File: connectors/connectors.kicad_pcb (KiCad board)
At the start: 2 copper layers, 41.7 x 4.8 mm, 15 parts, among them P11 CONN_1, P12 CONN_1, P13 CONN_1, P14 CONN_1, P15 CONN_1, P21 CONN_1, P22 CONN_1, P23 CONN_1, P24 CONN_1, P25 CONN_1

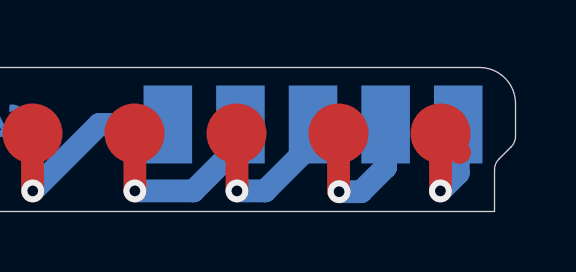
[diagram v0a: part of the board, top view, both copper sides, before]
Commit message: Remove extra track.
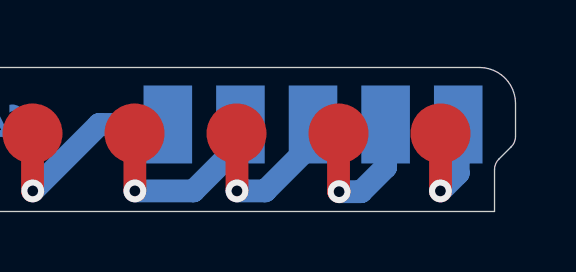
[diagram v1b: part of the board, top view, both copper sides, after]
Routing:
- net N-000005: track 5.27 -> 4.38 mm
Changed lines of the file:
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@@
     (links 5)
     (no_connects 0)
-    (area 108.5 78.745 182.728571 112.4385)
+    (area 108.5 78.745 182.728571 112.7285)
     (thickness 1.6)
     (drawings 25)
-    (tracks 32)
+    (tracks 31)
     (zones 0)
     (modules 15)
@@
   (segment (start 153.7208 108.9892) (end 153.723 108.987) (width 0.762) (layer B.Cu) (net 4))
   (segment (start 155.553 109.287) (end 155.553 111.1978) (width 0.762) (layer F.Cu) (net 5))
+  (segment (start 155.553 111.1978) (end 155.5496 111.2012) (width 0.762) (layer F.Cu) (net 5))
+  (via (at 155.5496 111.2012) (size 0.762) (drill 0.3556) (layers F.Cu B.Cu) (net 5))
+  (segment (start 155.5496 111.2012) (end 156.143 110.6078) (width 0.762) (layer B.Cu) (net 5))
   (segment (start 156.143 110.6078) (end 156.143 108.987) (width 0.762) (layer B.Cu) (net 5))
-  (segment (start 155.5496 111.2012) (end 156.143 110.6078) (width 0.762) (layer B.Cu) (net 5))
-  (via (at 155.5496 111.2012) (size 0.762) (drill 0.3556) (layers F.Cu B.Cu) (net 5))
-  (segment (start 155.553 111.1978) (end 155.5496 111.2012) (width 0.762) (layer F.Cu) (net 5))
-  (segment (start 155.553 109.287) (end 156.1846 109.9186) (width 0.762) (layer F.Cu) (net 5))
 )

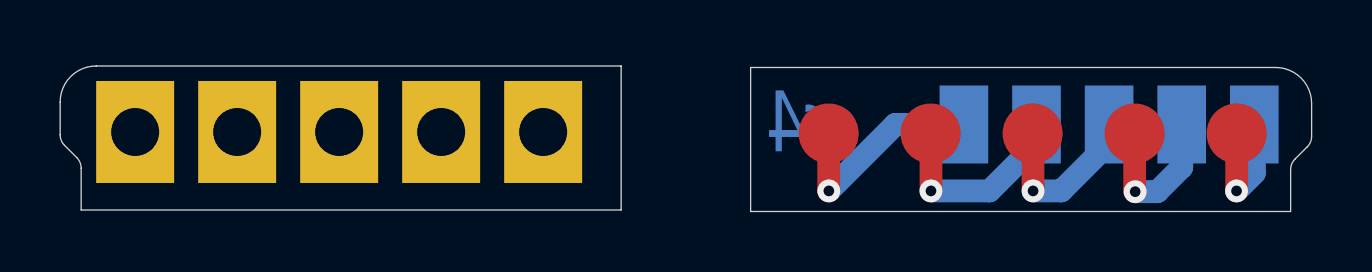
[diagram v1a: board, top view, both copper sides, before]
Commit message: Add drill holes to the connector.
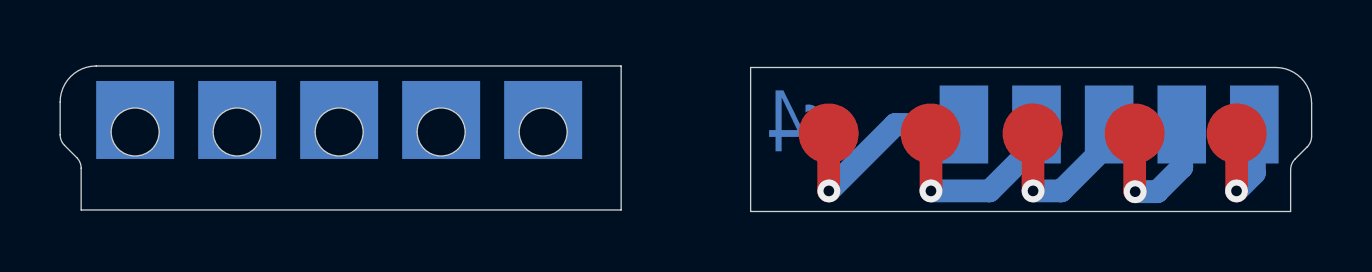
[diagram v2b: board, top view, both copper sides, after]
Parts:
- added REF**: VAL**, UGL:UHK_Connector_Left_Inner_Drill, F.Cu at (118.8, 109.2)
- added REF**: VAL**, UGL:UHK_Connector_Left_Inner_Drill, F.Cu at (122.2, 109.2)
- added REF**: VAL**, UGL:UHK_Connector_Left_Inner_Drill, F.Cu at (125.6, 109.2)
- added REF**: VAL**, UGL:UHK_Connector_Left_Inner_Drill, F.Cu at (129.0, 109.2)
- added REF**: VAL**, UGL:UHK_Connector_Left_Inner_Drill, F.Cu at (132.4, 109.2)
- moved REF** 0.40 mm to (122.2, 108.8)
- moved REF** 0.40 mm to (132.4, 108.8)
- moved REF** 0.40 mm to (125.6, 108.8)
- moved REF** 0.40 mm to (129.0, 108.8)
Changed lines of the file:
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@@
     (tracks 31)
     (zones 0)
-    (modules 15)
+    (modules 20)
     (nets 6)
   )
@@
     (mod_text_size 1.524 1.524)
     (mod_text_width 0.3048)
-    (pad_size 2.6 3.4)
-    (pad_drill 1.6)
+    (pad_size 2.6 2.6)
+    (pad_drill 0)
     (pad_to_mask_clearance 0)
     (aux_axis_origin 0 0)
@@
   )
   (module UGL:UHK_Connector_Left_Inner_Pad locked (layer B.Cu)
-    (at 132.437 109.237 180)
-    (fp_text reference REF** (at 0 2.54 180) (layer B.SilkS) hide
-      (effects (font (size 0.75 0.75) (thickness 0.15)) (justify mirror))
-    )
-    (fp_text value VAL** (at 0 -2.54 180) (layer B.SilkS) hide
-      (effects (font (size 0.75 0.75) (thickness 0.15)) (justify mirror))
-    )
-    (pad "" np_thru_hole rect (at 0 0 180) (size 2.6 3.4) (drill 1.6) (layers *.Cu *.Mask B.SilkS))
-  )
-  (module UGL:UHK_Connector_Left_Inner_Pad locked (layer B.Cu)
-    (at 129.037 109.237 180)
-    (fp_text reference REF** (at 0 2.54 180) (layer B.SilkS) hide
-      (effects (font (size 0.75 0.75) (thickness 0.15)) (justify mirror))
-    )
-    (fp_text value VAL** (at 0 -2.54 180) (layer B.SilkS) hide
-      (effects (font (size 0.75 0.75) (thickness 0.15)) (justify mirror))
-    )
-    (pad "" np_thru_hole rect (at 0 0 180) (size 2.6 3.4) (drill 1.6) (layers *.Cu *.Mask B.SilkS))
-  )
-  (module UGL:UHK_Connector_Left_Inner_Pad locked (layer B.Cu)
-    (at 125.637 109.237 180)
-    (fp_text reference REF** (at 0 2.54 180) (layer B.SilkS) hide
-      (effects (font (size 0.75 0.75) (thickness 0.15)) (justify mirror))
-    )
-    (fp_text value VAL** (at 0 -2.54 180) (layer B.SilkS) hide
-      (effects (font (size 0.75 0.75) (thickness 0.15)) (justify mirror))
-    )
-    (pad "" np_thru_hole rect (at 0 0 180) (size 2.6 3.4) (drill 1.6) (layers *.Cu *.Mask B.SilkS))
-  )
-  (module UGL:UHK_Connector_Left_Inner_Pad locked (layer B.Cu)
-    (at 122.237 109.237 180)
-    (fp_text reference REF** (at 0 2.54 180) (layer B.SilkS) hide
-      (effects (font (size 0.75 0.75) (thickness 0.15)) (justify mirror))
-    )
-    (fp_text value VAL** (at 0 -2.54 180) (layer B.SilkS) hide
-      (effects (font (size 0.75 0.75) (thickness 0.15)) (justify mirror))
-    )
-    (pad "" np_thru_hole rect (at 0 0 180) (size 2.6 3.4) (drill 1.6) (layers *.Cu *.Mask B.SilkS))
+    (at 122.237 108.837 180)
+    (fp_text reference REF** (at 0 2.54 180) (layer B.SilkS) hide
+      (effects (font (size 0.75 0.75) (thickness 0.15)) (justify mirror))
+    )
+    (fp_text value VAL** (at 0 -2.54 180) (layer B.SilkS) hide
+      (effects (font (size 0.75 0.75) (thickness 0.15)) (justify mirror))
+    )
+    (pad "" smd rect (at 0 0 180) (size 2.6 2.6) (layers B.Cu B.Paste B.Mask))
   )
   (module UGL:UHK_Connector_Left_Inner_Pad locked (layer B.Cu)
@@
       (effects (font (size 0.75 0.75) (thickness 0.15)) (justify mirror))
     )
-    (pad "" np_thru_hole rect (at 0 0 180) (size 2.6 3.4) (drill 1.6) (layers *.Cu *.Mask B.SilkS))
+    (pad "" smd rect (at 0 0.4 180) (size 2.6 2.6) (layers B.Cu B.Paste B.Mask))
   )
   (module UGL:UHK_Connector_Right_Inner_Pad locked (layer B.Cu)
@@
       (net 5 N-000005))
   )
+  (module UGL:UHK_Connector_Left_Inner_Drill locked (layer F.Cu)
+    (at 118.837 109.237)
+    (fp_text reference REF** (at 0 -1.905) (layer F.SilkS) hide
+      (effects (font (size 0.75 0.75) (thickness 0.15)))
+    )
+    (fp_text value VAL** (at 0 1.905) (layer F.SilkS) hide
+      (effects (font (size 0.75 0.75) (thickness 0.15)))
+    )
+    (pad "" np_thru_hole circle (at 0 0) (size 1.6 1.6) (drill 1.6) (layers *.Cu *.Mask F.SilkS))
+  )
+  (module UGL:UHK_Connector_Left_Inner_Drill locked (layer F.Cu)
+    (at 122.237 109.237)
+    (fp_text reference REF** (at 0 -1.905) (layer F.SilkS) hide
+      (effects (font (size 0.75 0.75) (thickness 0.15)))
+    )
+    (fp_text value VAL** (at 0 1.905) (layer F.SilkS) hide
+      (effects (font (size 0.75 0.75) (thickness 0.15)))
+    )
+    (pad "" np_thru_hole circle (at 0 0) (size 1.6 1.6) (drill 1.6) (layers *.Cu *.Mask F.SilkS))
+  )
+  (module UGL:UHK_Connector_Left_Inner_Drill locked (layer F.Cu)
+    (at 125.637 109.237)
+    (fp_text reference REF** (at 0 -1.905) (layer F.SilkS) hide
+      (effects (font (size 0.75 0.75) (thickness 0.15)))
+    )
+    (fp_text value VAL** (at 0 1.905) (layer F.SilkS) hide
+      (effects (font (size 0.75 0.75) (thickness 0.15)))
+    )
+    (pad "" np_thru_hole circle (at 0 0) (size 1.6 1.6) (drill 1.6) (layers *.Cu *.Mask F.SilkS))
+  )
+  (module UGL:UHK_Connector_Left_Inner_Drill locked (layer F.Cu)
+    (at 129.037 109.237)
+    (fp_text reference REF** (at 0 -1.905) (layer F.SilkS) hide
+      (effects (font (size 0.75 0.75) (thickness 0.15)))
+    )
+    (fp_text value VAL** (at 0 1.905) (layer F.SilkS) hide
+      (effects (font (size 0.75 0.75) (thickness 0.15)))
+    )
+    (pad "" np_thru_hole circle (at 0 0) (size 1.6 1.6) (drill 1.6) (layers *.Cu *.Mask F.SilkS))
+  )
+  (module UGL:UHK_Connector_Left_Inner_Drill locked (layer F.Cu)
+    (at 132.437 109.237)
+    (fp_text reference REF** (at 0 -1.905) (layer F.SilkS) hide
+      (effects (font (size 0.75 0.75) (thickness 0.15)))
+    )
+    (fp_text value VAL** (at 0 1.905) (layer F.SilkS) hide
+      (effects (font (size 0.75 0.75) (thickness 0.15)))
+    )
+    (pad "" np_thru_hole circle (at 0 0) (size 1.6 1.6) (drill 1.6) (layers *.Cu *.Mask F.SilkS))
+  )
+  (module UGL:UHK_Connector_Left_Inner_Pad locked (layer B.Cu)
+    (at 125.637 108.837 180)
+    (fp_text reference REF** (at 0 2.54 180) (layer B.SilkS) hide
+      (effects (font (size 0.75 0.75) (thickness 0.15)) (justify mirror))
+    )
+    (fp_text value VAL** (at 0 -2.54 180) (layer B.SilkS) hide
+      (effects (font (size 0.75 0.75) (thickness 0.15)) (justify mirror))
+    )
+    (pad "" smd rect (at 0 0 180) (size 2.6 2.6) (layers B.Cu B.Paste B.Mask))
+  )
+  (module UGL:UHK_Connector_Left_Inner_Pad locked (layer B.Cu)
+    (at 129.037 108.837 180)
+    (fp_text reference REF** (at 0 2.54 180) (layer B.SilkS) hide
+      (effects (font (size 0.75 0.75) (thickness 0.15)) (justify mirror))
+    )
+    (fp_text value VAL** (at 0 -2.54 180) (layer B.SilkS) hide
+      (effects (font (size 0.75 0.75) (thickness 0.15)) (justify mirror))
+    )
+    (pad "" smd rect (at 0 0 180) (size 2.6 2.6) (layers B.Cu B.Paste B.Mask))
+  )
+  (module UGL:UHK_Connector_Left_Inner_Pad locked (layer B.Cu)
+    (at 132.437 108.837 180)
+    (fp_text reference REF** (at 0 2.54 180) (layer B.SilkS) hide
+      (effects (font (size 0.75 0.75) (thickness 0.15)) (justify mirror))
+    )
+    (fp_text value VAL** (at 0 -2.54 180) (layer B.SilkS) hide
+      (effects (font (size 0.75 0.75) (thickness 0.15)) (justify mirror))
+    )
+    (pad "" smd rect (at 0 0 180) (size 2.6 2.6) (layers B.Cu B.Paste B.Mask))
+  )
   (gr_line (start 145.253 107.087) (end 145.253 111.887) (angle 90) (layer Dwgs.User) (width 0.01))
